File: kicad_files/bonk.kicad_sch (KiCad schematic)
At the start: 21 parts, among them J1 Conn_01x04, J2 Conn_01x02, J3 Conn_01x04, SW1 SW_Push, U1 XC6206PxxxMR, U2 STM32F072CBTx

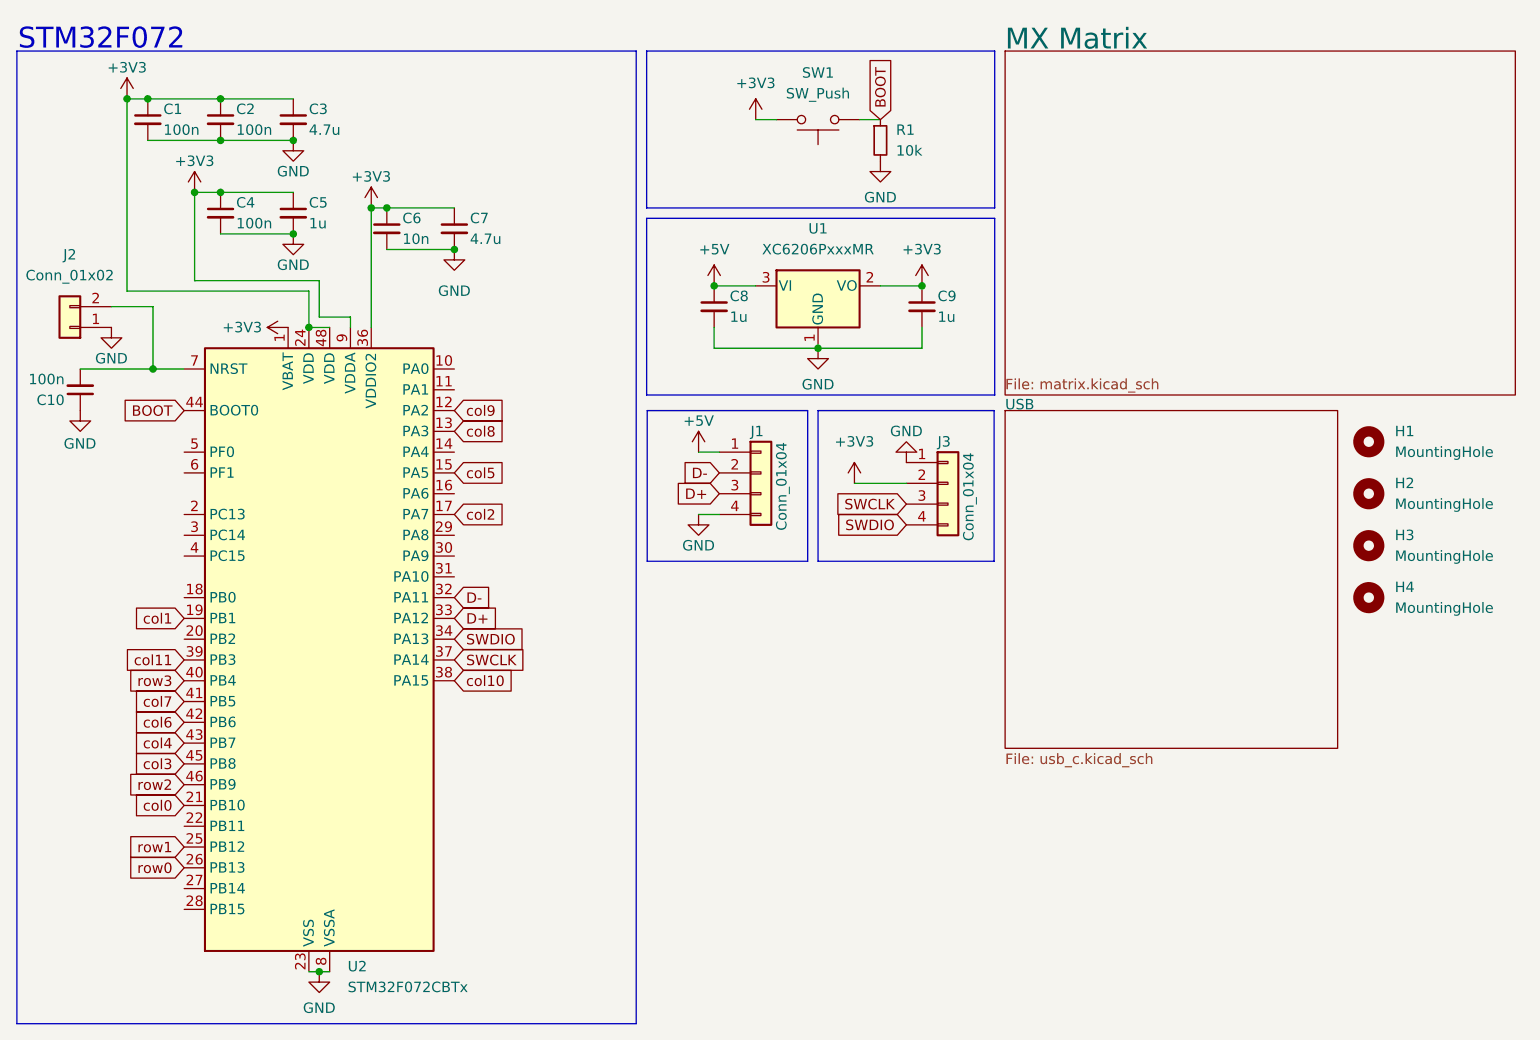
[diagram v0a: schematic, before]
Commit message: rev1.1
1. Changed reset/boot circuitry to have single-button Reset/Boot functionality.
2. Removed mounting holes
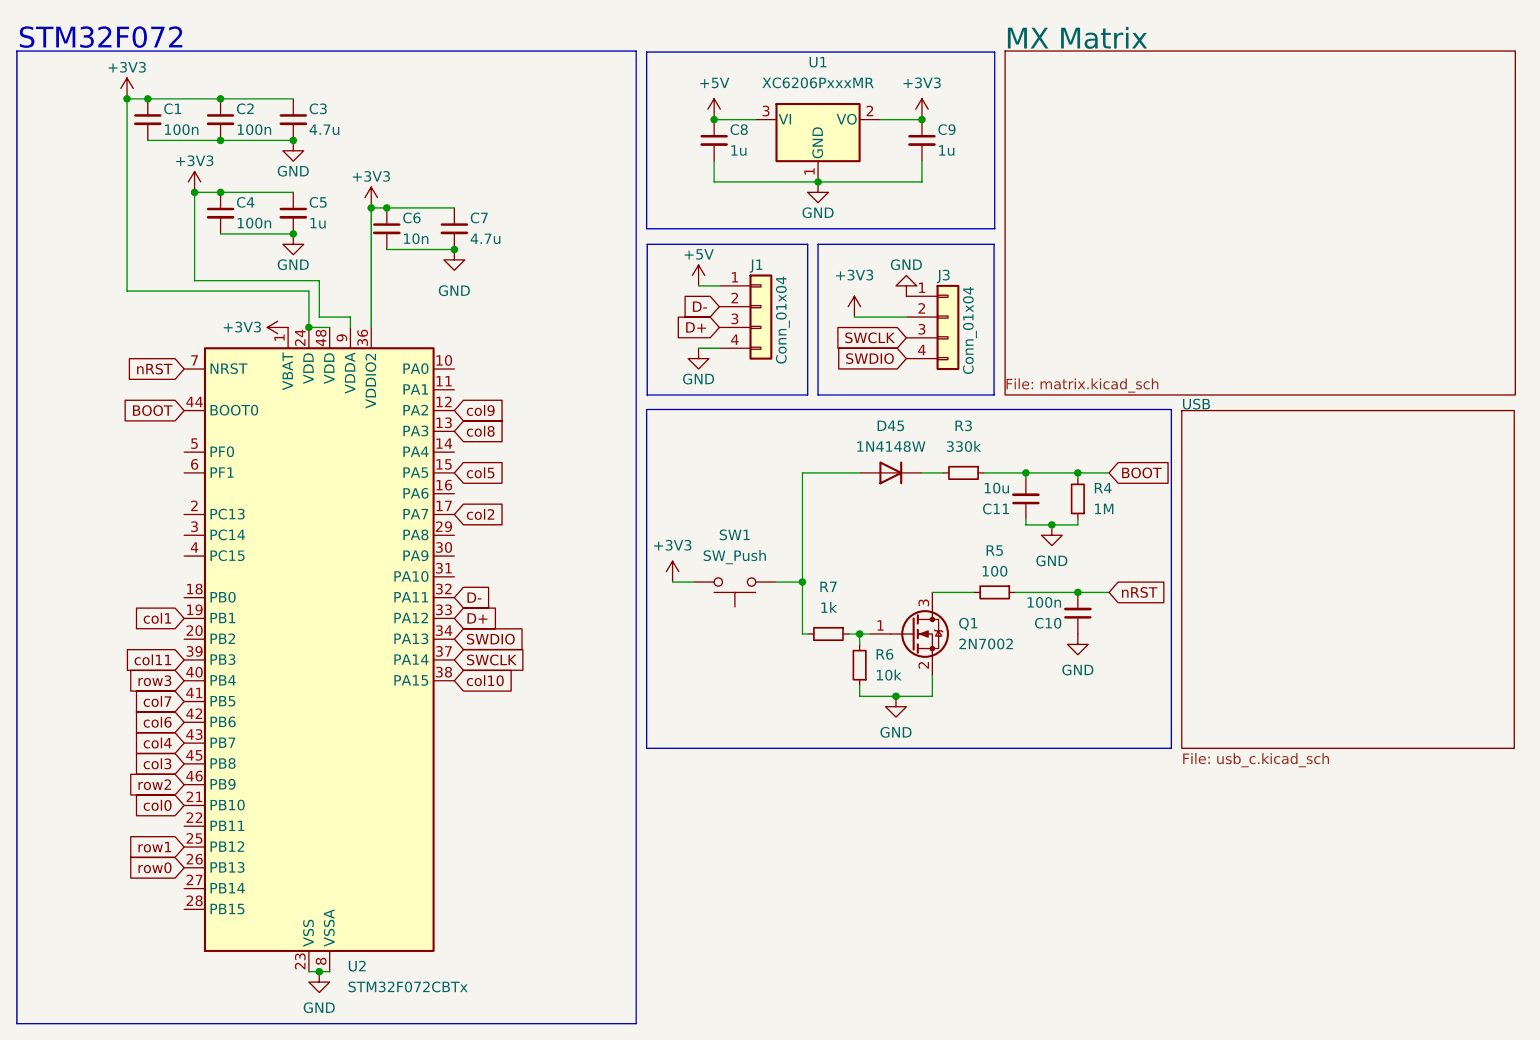
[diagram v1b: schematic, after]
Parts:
- removed H1, H2, H3, H4: MountingHole, MountingHole:MountingHole_3.2mm_M3, symbol Mechanical:MountingHole
- removed J2: Conn_01x02, Connector_PinHeader_2.54mm:PinHeader_1x02_P2.54mm_Vertical, symbol Connector_Generic:Conn_01x02
- added C11: 10u, Capacitor_SMD:C_0603_1608Metric, symbol Device:C_Small
- added D45: 1N4148W, Diode_SMD:D_SOD-123, symbol Diode:1N4148W
- added Q1: 2N7002, Package_TO_SOT_SMD:SOT-23, symbol Transistor_FET:2N7002
- added R3: 330k, Resistor_SMD:R_0805_2012Metric, symbol Device:R_Small
- added R5: 100, Resistor_SMD:R_0402_1005Metric_Pad0.72x0.64mm_HandSolder, symbol Device:R_Small
- added R6: 10k, Resistor_SMD:R_0603_1608Metric_Pad0.98x0.95mm_HandSolder, symbol Device:R_Small
- added R7: 1k, Resistor_SMD:R_0603_1608Metric, symbol Device:R_Small
- R4: renamed from R1; value 10k -> 1M; footprint Resistor_SMD:R_0603_1608Metric -> Resistor_SMD:R_0805_2012Metric
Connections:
- net BOOT: now also R4.2, C11.2, R3.1; no longer R4.1, SW1.1
- net GND: now also R4.1, C11.1, Q1.2 (S), R6.1; no longer R4.2
- net nRST: now reaches C10.2, U2.7 (NRST)
- net nRST: now also R5.1
- new net: D45.2 (A), R7.2, SW1.1
- new net: Q1.1 (G), R6.2, R7.1
- new net: Q1.3 (D), R5.2
- new net: D45.1 (K), R3.2
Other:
- moved on the sheet: C10, C8, C9, J1, J3, R4, SW1, U1
